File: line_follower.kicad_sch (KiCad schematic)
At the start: 54 parts, among them J1 Conn_01x20_Socket, J10 Conn_01x20_Pin, J11 Conn_01x20_Pin, J2 Conn_01x20_Socket, J3 Conn_01x06_Socket, J4 Conn_01x06_Socket, J5 XT60-M, J6 Conn_01x02_Socket, J7 Conn_01x02_Socket, J8 Conn_01x06_Socket, J9 MOTOR OUTPUTS, SW1 SW_Push, SW2 SW_Push, SW3 SW_Push, SW4 SW_Push, SW5 SW_Push, SW6 SW_Push, SW7 SW_Push

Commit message: schematic updated by veena
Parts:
- removed C5, C7: 0.1u, symbol Device:C
- added D10, D2, D3, D4, D5, D6, D7, D8, D9: LED, symbol Device:LED
- added F1: Polyfuse, symbol Device:Polyfuse
- added R20, R21, R22, R23, R24, R25, R26, R27, R28: 220, symbol Device:R
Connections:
- net PA10 is gone; now on net IN2: J10.7 (Pin_7), J2.7 (Pin_7)
- net PA11 is gone; now on net IN3: J10.8 (Pin_8), J2.8 (Pin_8)
- net PA12 is gone; now on net IN4: J10.9 (Pin_9), J2.9 (Pin_9)
- net PA8 is gone; now on net EEP: J10.5 (Pin_5), J2.5 (Pin_5)
- net PA9 is gone; now on net IN1: J10.6 (Pin_6), J2.6 (Pin_6)
- net PB12 is gone; now on net CALIB: J10.1 (Pin_1), J2.1 (Pin_1)
- net PB13 is gone; now on net LEFT : J10.2 (Pin_2), J2.2 (Pin_2)
- net 3.3V_STM: now also J10.20 (Pin_20), J11.3 (Pin_3)
- net 5V_STM: now also J10.18 (Pin_18), J11.1 (Pin_1)
- net BUCK_IN: now also F1.2; no longer SW1.2
- net CALIB: no longer J1.8 (Pin_8)
- net EEP: no longer J1.10 (Pin_10)
- net EN: now also J10.16 (Pin_16)
- net GND: now also J10.19 (Pin_19), J11.2 (Pin_2), R20.2, R21.2, R22.2, R23.2, R24.2, R25.2, R26.2, R27.2, R28.2
- net IN1: no longer J1.14 (Pin_14)
- net IN2: no longer J1.13 (Pin_13)
- net IN3: no longer J1.12 (Pin_12)
- net IN4: no longer J1.11 (Pin_11)
- net LEFT : no longer J1.7 (Pin_7)
- net NRST: now also J11.16 (Pin_16)
- net PA0: now also A1.4, J11.15 (Pin_15), R2.1
- net PA15: now also J10.10 (Pin_10)
- net PA6: now also A7.4, J11.9 (Pin_9), R8.1
- net PB1: now also J11.6 (Pin_6); no longer SW6.2
- net PB10: now also J11.4 (Pin_4)
- net PB14: now also SW6.2
- net PB15: now also SW7.2
- net PB2: now also J11.5 (Pin_5); no longer SW7.2
- net PB3: now also J10.11 (Pin_11)
- net PB4: now also J10.12 (Pin_12)
- net PB5: now also J10.13 (Pin_13)
- net PB6: now also J10.14 (Pin_14)
- net PB7: now also J10.15 (Pin_15)
- net PB9: now also J10.17 (Pin_17)
- net PC13: now also J11.19 (Pin_19)
- net PC14: now also J11.18 (Pin_18)
- net PC15: now also J11.17 (Pin_17)
- net VBAT_STM: now also J11.20 (Pin_20)
- net PA4: now reaches A5.4, R6.1
- net PA4: now also J1.11 (Pin_11), J11.11 (Pin_11)
- net PA1: now reaches A2.4, R3.1
- net PA1: now also J1.14 (Pin_14), J11.14 (Pin_14)
- net PB0: now reaches A9.4, R10.1
- net PB0: now also J1.7 (Pin_7), J11.7 (Pin_7)
- net PA3: now reaches A4.4, R5.1
- net PA3: now also J1.12 (Pin_12), J11.12 (Pin_12)
- net PA5: now reaches A6.4, R7.1
- net PA5: now also J1.10 (Pin_10), J11.10 (Pin_10)
- net PA2: now reaches J11.13 (Pin_13)
- net PA2: now also A3.4, J1.13 (Pin_13), R4.1
- net PA7: now reaches J11.8 (Pin_8)
- net PA7: now also A8.4, J1.8 (Pin_8), R9.1
- net pow_led-: now reaches D1.1 (K), R1.1
- new net: D3.1 (K), R21.1
- new net: D5.1 (K), R23.1
- new net: D9.1 (K), R27.1
- new net: D4.1 (K), R22.1
- new net: D8.1 (K), R26.1
- new net: D10.1 (K), R28.1
- new net: D6.1 (K), R24.1
- new net: D7.1 (K), R25.1
- new net: D2.1 (K), R20.1
- new net FUSE : F1.1, SW1.2
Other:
- note added: "FUSE"
- moved on the sheet: A1, A2, A3, A4, A5, A6, A7, A8, A9, R11, R12, R13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

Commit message: schematic updated by veena
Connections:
- net PB1 is gone; now on net CALIB: J1.6 (Pin_6), J11.6 (Pin_6)
- net PC15 is gone; now on net LEFT : J1.17 (Pin_17), J11.17 (Pin_17)
- net BAT+: now also F1.1; no longer SW1.1
- net BUCK_IN: now also SW1.2; no longer F1.2
- net CALIB: no longer J10.1 (Pin_1), J2.1 (Pin_1)
- net EEP: now also J10.4 (Pin_4), J2.4 (Pin_4); no longer J10.5 (Pin_5), J2.5 (Pin_5)
- net IN1: now also J10.5 (Pin_5), J2.5 (Pin_5); no longer J10.6 (Pin_6), J2.6 (Pin_6)
- net IN2: now also J10.6 (Pin_6), J2.6 (Pin_6); no longer J10.7 (Pin_7), J2.7 (Pin_7)
- net IN3: now also J10.7 (Pin_7), J2.7 (Pin_7); no longer J10.8 (Pin_8), J2.8 (Pin_8)
- net IN4: now also J10.8 (Pin_8), J2.8 (Pin_8); no longer J10.9 (Pin_9), J2.9 (Pin_9)
- net LEFT : no longer J10.2 (Pin_2), J2.2 (Pin_2)
- net PA15: now also D6.2 (A)
- net PB10: now also D9.2 (A)
- net PB14: now also D4.2 (A); no longer SW6.2
- net PB2: now also D10.2 (A)
- net PB3: now also D7.2 (A)
- net PB4: now also D8.2 (A)
- net PC13: now also SW7.2
- net PC14: now also SW6.2
- net PA12: now reaches D5.2 (A)
- net PA12: now also J10.9 (Pin_9), J2.9 (Pin_9)
- net PB12: now reaches D2.2 (A)
- net PB12: now also J10.1 (Pin_1), J2.1 (Pin_1)
- net PB13: now reaches D3.2 (A)
- net PB13: now also J10.2 (Pin_2), J2.2 (Pin_2)
- removed net FUSE : F1.1, SW1.2
- removed net PB15: J10.4 (Pin_4), J2.4 (Pin_4), SW7.2
- new net FUSE_OUT : F1.2, SW1.1
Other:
- note added: "LEDS FOR CALIBRATION STATUS"

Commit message: schematic updated by veena
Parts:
- added C10, C11, C12, C13, C14, C15, C16, C6, C7, C8, C9: 0.1u, symbol Device:C
- renumbered C6 to C5
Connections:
- net 3.3V_STM: now also C11.2, C12.2, C13.2, C14.2, C15.2
- net 5V_STM: now also C10.2, C6.2, C7.2, C8.2, C9.2
- net GND: now also C10.1, C11.1, C12.1, C13.1, C14.1, C15.1, C16.1, C6.1, C7.1, C8.1, C9.1
- net STM_KILL: now also C16.2
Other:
- moved on the sheet: A1, A2, A3, A4, A5, A6, A7, A8, A9, C1, C2, C3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

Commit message: minor changes
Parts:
- removed SW2: SW_Push, symbol Switch:SW_Push
- added C17, C18, C19, C20, C21: C, symbol Device:C
- C10, C11, C12, C13, C14, C15, C16, C3, C5, C6, C7, C8, C9: value 0.1u -> C
- R10, R2, R3, R4, R5, R6, R7, R8, R9: value 47k -> 220
- R11, R12, R13, R14, R15, R16, R17, R18, R19: value 220 -> 47k
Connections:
- net 3.3V_STM: now also C10.1, C11.1, C12.1, C3.1, C5.1, C6.1, C7.1, C8.1, C9.1, R10.1, R2.1, R3.1, R4.1, R5.1, R6.1, R7.1, R8.1, R9.1; no longer C11.2, C12.2, C13.2, C14.2, C15.2, R10.2, R2.2, R3.2, R4.2, R5.2, R6.2, R7.2, R8.2, R9.2
- net 5V_STM: now also C1.2, C13.1, C14.1, C15.1, C16.1, J7.1 (Pin_1), R11.1, R12.1, R13.1, R14.1, R15.1, R16.1, R17.1, R18.1, R19.1, C17.1, C18.1, C19.1, C20.1, C21.1; no longer A1.1, A2.1, A3.1, A4.1, A5.1, A6.1, A7.1, A8.1, A9.1, C10.2, C5.2, C6.2, C7.2, C8.2, C9.2
- net BAT+: no longer C1.2
- net BUCK_IN: no longer C3.2
- net GND: now also A1.2, A2.2, A3.2, A4.2, A5.2, A6.2, A7.2, A8.2, A9.2, C10.2, C11.2, C12.2, C13.2, C14.2, C15.2, C16.2, C3.2, C5.2, C6.2, C7.2, C8.2, C9.2, C17.2, C18.2, C19.2, C20.2, C21.2; no longer C10.1, C11.1, C12.1, C13.1, C14.1, C15.1, C16.1, C3.1, C5.1, C6.1, C7.1, C8.1, C9.1, R11.1, R12.1, R13.1, R14.1, R15.1, R16.1, R17.1, R18.1, R19.1
- net PA0: now also R11.2; no longer R2.1
- net PA1: now also R12.2; no longer R3.1
- net PA2: now also R13.2; no longer R4.1
- net PA3: now also R14.2; no longer R5.1
- net PA4: now also R15.2; no longer R6.1
- net PA5: now also R16.2; no longer R7.1
- net PA6: now also R17.2; no longer R8.1
- net PA7: now also R18.2; no longer R9.1
- net PB0: now also R19.2; no longer R10.1
- removed net STM_KILL: C16.2, J7.1 (Pin_1)
- new net: A2.1, R3.2
- new net: A8.1, R9.2
- new net: A1.1, R2.2
- new net: A6.1, R7.2
- new net: A7.1, R8.2
- new net: A4.1, R5.2
- new net: A5.1, R6.2
- new net: A3.1, R4.2
- new net: A9.1, R10.2
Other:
- note added: "Decoupling capacitors for RPR220"
- note added: "Decoupling caps"
- note added: "For only motor"
- note added: "For whole bot"
- note added: "MISC Buttons"
- note added: "Modules"
- note added: "Power Components"
- note added: "Resistors for collector of RPR220 for sensitivity"
- note added: "Sensor Array Unit"
- note removed: "MOTOR KILL SWITCH"
- moved on the sheet: A1, A2, A3, A4, A5, A6, A7, A8, A9, C2, C4, D1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

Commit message: minor changes
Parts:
- added D11, D12, D13, D14: LED, symbol Device:LED
- added R29, R30, R31, R32: 220, symbol Device:R
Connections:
- net 3.3V_STM: now also SW3.2, SW5.1, SW6.1, SW7.1
- net CALIB: now also J1.15 (Pin_15), J11.15 (Pin_15), R11.2, D14.2 (A); no longer J1.6 (Pin_6), J11.6 (Pin_6)
- net GND: now also R29.2, R30.2, R31.2, R32.2; no longer SW3.2, SW5.1, SW6.1, SW7.1
- net LEFT : now also D11.2 (A)
- net PA1: now also A1.4; no longer A2.4
- net PA2: now also A2.4; no longer A3.4
- net PA3: now also A3.4; no longer A4.4
- net PA4: now also A4.4; no longer A5.4
- net PA5: now also A5.4; no longer A6.4
- net PA6: now also A6.4; no longer A7.4
- net PA7: now also A7.4; no longer A8.4
- net PB0: now also A8.4; no longer A9.4
- net PC13: now also D13.2 (A)
- net PC14: now also D12.2 (A)
- removed net PA0: A1.4, J1.15 (Pin_15), J11.15 (Pin_15), R11.2
- new net: D11.1 (K), R29.1
- new net: D14.1 (K), R32.1
- new net: D13.1 (K), R31.1
- new net: D12.1 (K), R30.1
- new net PB1: A9.4, J1.6 (Pin_6), J11.6 (Pin_6)
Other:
- moved on the sheet: C2, D10, D4, D7, J3, J4, J8, J9, R22, R25, R28, SW3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

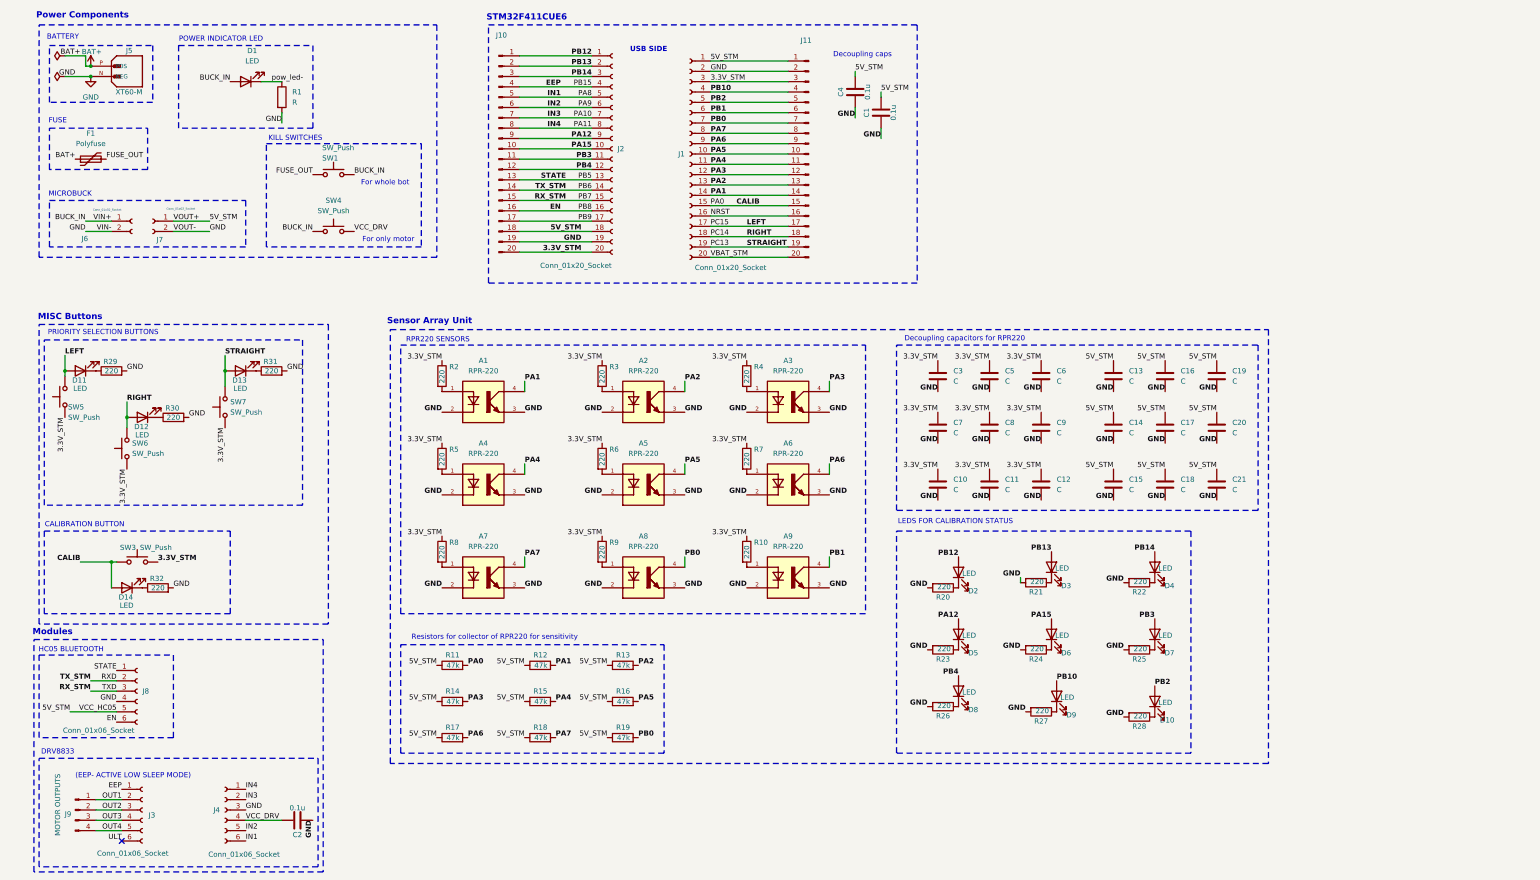
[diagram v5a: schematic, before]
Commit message: assigned footprints
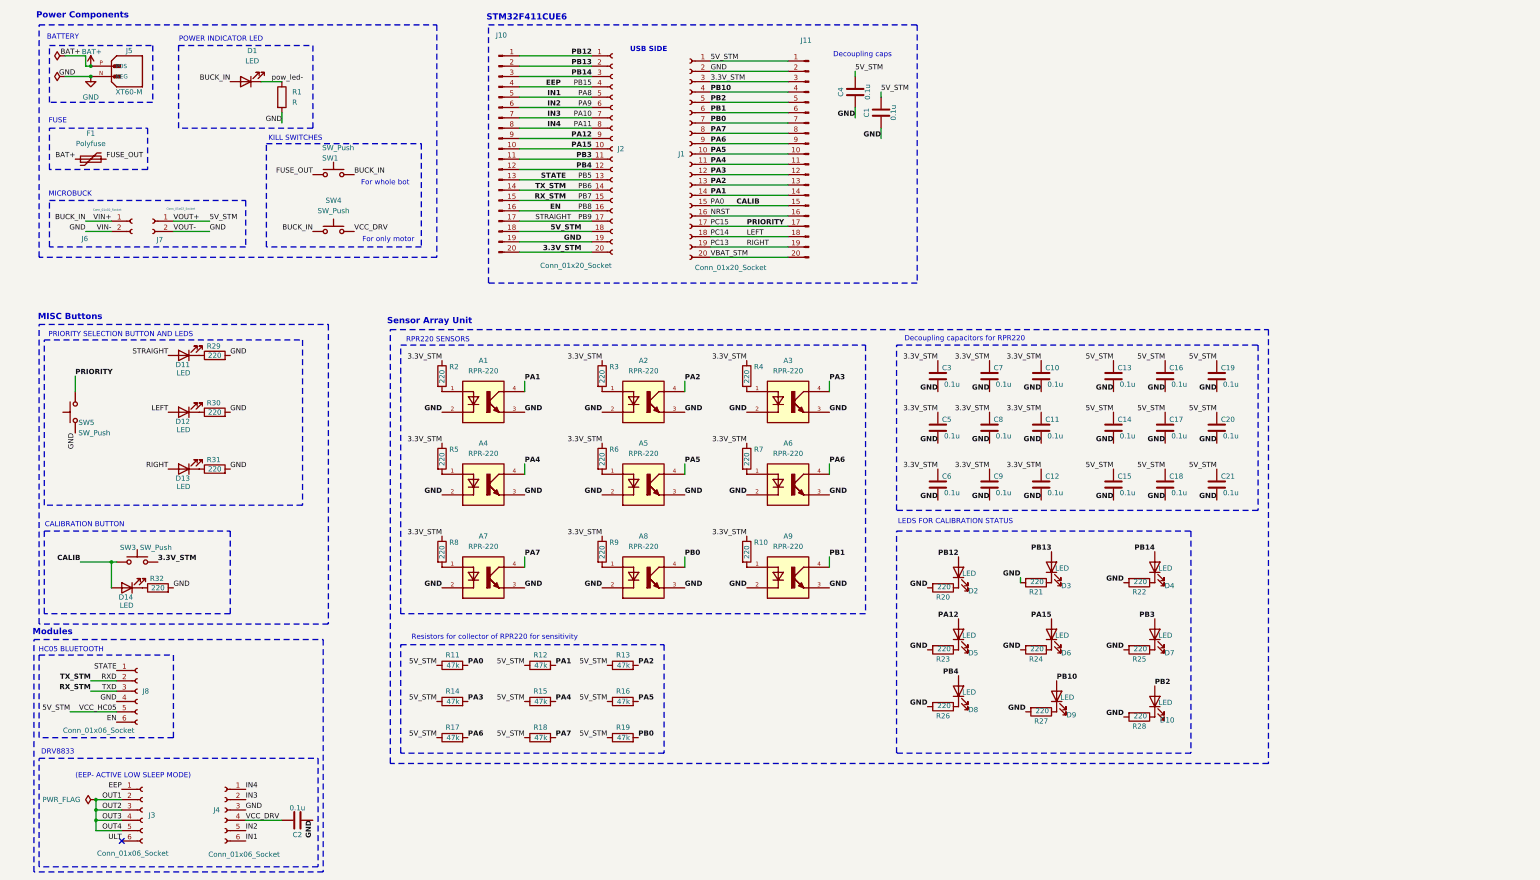
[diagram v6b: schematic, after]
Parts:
- removed J9: MOTOR OUTPUTS, symbol Connector:Conn_01x04_Pin
- removed SW6, SW7: SW_Push, symbol Switch:SW_Push
- C1, C2, C4: footprint (none) -> Capacitor_SMD:C_0603_1608Metric_Pad1.08x0.95mm_HandSolder
- C10, C11, C12, C13, C14, C15, C16, C17, C18, C19, C20, C21, C3, C5, C6, C7, C8, C9: value C -> 0.1u; footprint (none) -> Capacitor_SMD:C_0603_1608Metric_Pad1.08x0.95mm_HandSolder
- D1, D10, D11, D12, D13, D14, D2, D3, D4, D5, D6, D7, D8, D9: footprint (none) -> LED_SMD:LED_0603_1608Metric_Pad1.05x0.95mm_HandSolder
- J1, J10, J11, J2: footprint (none) -> Connector_PinSocket_2.54mm:PinSocket_1x20_P2.54mm_Vertical_SMD_Pin1Left
- J3, J4, J8: footprint (none) -> Connector_PinSocket_2.54mm:PinSocket_1x06_P2.54mm_Vertical_SMD_Pin1Left
- R1, R10, R11, R12, R13, R14, R15, R16, R17, R18, R19, R2, R20, R21, R22, R23, R24, R25, R26, R27, R28, R29, R3, R30, R31, R32, R4, R5, R6, R7, R8, R9: footprint (none) -> Resistor_SMD:R_0603_1608Metric_Pad0.98x0.95mm_HandSolder
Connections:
- net OUT2 is gone; now on net OUT1: J3.3 (Pin_3)
- net OUT3 is gone; now on net OUT1: J3.4 (Pin_4)
- net OUT4 is gone; now on net OUT1: J3.5 (Pin_5)
- net 3.3V_STM: no longer SW5.1
- net GND: now also SW5.1
- net PB9: now also D11.2 (A)
- net LEFT  renamed PC15
- net PC15: no longer D11.2 (A)
- net PC14 renamed LEFT
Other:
- note added: "PRIORITY SELECTION BUTTON AND LEDS"
- note removed: "PRIORITY SELECTION BUTTONS"
- moved on the sheet: D11, R29, SW5

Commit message: schematic complete
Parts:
- added J12, J9: Conn_01x02_Socket, Connector_PinSocket_2.54mm:PinSocket_1x02_P2.54mm_Vertical, symbol Connector:Conn_01x02_Socket
- D1, D10, D11, D12, D13, D14, D2, D3, D4, D5, D6, D7, D8, D9: footprint LED_SMD:LED_0603_1608Metric_Pad1.05x0.95mm_HandSolder -> LED_SMD:LED_0805_2012Metric_Pad1.15x1.40mm_HandSolder
- F1: footprint (none) -> Resistor_SMD:R_1812_4532Metric_Pad1.30x3.40mm_HandSolder
- J1, J2: footprint Connector_PinSocket_2.54mm:PinSocket_1x20_P2.54mm_Vertical_SMD_Pin1Left -> Connector_PinSocket_2.54mm:PinSocket_1x20_P2.54mm_Vertical
- J10, J11: footprint Connector_PinSocket_2.54mm:PinSocket_1x20_P2.54mm_Vertical_SMD_Pin1Left -> Connector_PinHeader_2.54mm:PinHeader_1x20_P2.54mm_Vertical
- J3, J4, J8: footprint Connector_PinSocket_2.54mm:PinSocket_1x06_P2.54mm_Vertical_SMD_Pin1Left -> Connector_PinSocket_2.54mm:PinSocket_1x06_P2.54mm_Vertical
- J5: footprint XT60-M:AMASS_XT60-M -> Connector_AMASS:AMASS_XT60-M_1x02_P7.20mm_Vertical
- J6, J7: footprint (none) -> Connector_PinSocket_2.54mm:PinSocket_1x02_P2.54mm_Vertical
- SW1, SW3, SW4: footprint (none) -> Button_Switch_THT:SW_Push_2P2T_Toggle_CK_PVA2xxH3xxxxxxV2
- SW5: footprint (none) -> Button_Switch_THT:SW_PUSH_6mm_H5mm
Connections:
- net 5V_STM: now also J7.2 (Pin_2)
- net BUCK_IN: now also J6.2 (Pin_2)
- net GND: now also J12.1 (Pin_1), J12.2 (Pin_2), J9.1 (Pin_1), J9.2 (Pin_2); no longer J6.2 (Pin_2), J7.2 (Pin_2)

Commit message: some placement done
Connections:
- net CALIB: no longer R11.2
- net PA1: now also R11.2; no longer R12.2
- net PA2: now also R12.2; no longer R13.2
- net PA3: now also R13.2; no longer R14.2
- net PA4: now also R14.2; no longer R15.2
- net PA5: now also R15.2; no longer R16.2
- net PA6: now also R16.2; no longer R17.2
- net PA7: now also R17.2; no longer R18.2
- net PB0: now also R18.2; no longer R19.2
- net PB1: now also R19.2
